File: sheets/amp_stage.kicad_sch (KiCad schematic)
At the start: 0 parts

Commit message: Complete Sheet 4 - Amp Stage TAS3251
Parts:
- added C34, C35, C38, C39, C40, C41, C42, C43, C44, C45: 1uF, symbol Device:C
- added C36, C37: 100nF, symbol Device:C
- added C46, C47, C48, C49: 33nF, symbol Device:C
- added C50, C51, C52, C53: 0.68µF, symbol Device:C
- added C54: 10nF, symbol Device:C
- added J2: Speaker Terminals, symbol Connector:Screw_Terminal_01x04
- added L4, L5, L6, L7: 15µH, symbol Device:L
- added R28, R29, R30, R31: 0.15, symbol Device:R
- added R32: 27K, symbol Device:R
- added R33: 10K, symbol Device:R
- added U10: TAS3251DKQR, DKQ0056A, symbol poe-aes67-amp:TAS3251DKQR
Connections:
- new net: C53.2, R31.1
- new net: R33.1, U10.18 (FREQ_ADJ)
- new net: C46.2, L4.1, U10.41 (SPK_OUTA+)
- new net: C45.1, U10.8 (CP)
- new net: C45.2, U10.6 (CN)
- new net: C51.2, R29.1
- new net: C47.1, U10.43 (BST_A-)
- new net: C47.2, L5.1, U10.39 (SPK_OUTA-)
- new net: C37.2, U10.12 (GVDD_A)
- new net: C48.2, L6.1, U10.36 (SPK_OUTB+)
- new net: C50.2, R28.1
- new net: U10.10 (DGND), U10.55 (AGND)
- new net: C40.2, U10.11 (DVDD_REG)
- new net: R32.2, U10.17 (OC_ADJ)
- new net: C39.2, U10.21 (DVDD)
- new net: C38.2, U10.23 (AVDD)
- new net: C54.1, U10.24 (C_START)
- new net: C36.2, U10.30 (GVDD_B)
- new net: C49.1, U10.31 (BST_B-)
- new net: C48.1, U10.32 (BST_B+)
- new net: C49.2, L7.1, U10.34 (SPK_OUTB-)
- new net: C46.1, U10.44 (BST_A+)
- new net: C41.1, U10.5 (CPVSS)
- new net: C52.2, R30.1
- new net +3.3V: C42.1, C43.1, C44.1, U10.52 (DAC_DVDD), U10.56 (DAC_AVDD), U10.9 (DAC_DVDD)
- new net AMP_CLIP (Output): U10.29 (CLIP_OTW_N)
- new net AMP_FAULT (Output): U10.28 (FAULT_N)
- new net AMP_MUTE (Input): U10.45 (DAC_MUTE_N)
- new net AMP_RESET (Input): U10.27 (RESET_AMP_N)
- new net GND: C34.1, C35.1, C36.1, C37.1, C38.1, C39.1, C40.1, C41.2, C42.2, C43.2, C44.2, C54.2, R28.2, R29.2, R30.2, R31.2, R32.1, R33.2, U10.13 (GND), U10.14 (MODE), U10.22 (GND), U10.33 (GND), U10.37 (GND), U10.38 (GND), U10.42 (GND), U10.46 (ADR), U10.7 (GND)
- new net I2C_SCL: U10.53 (SCL)
- new net I2C_SDA: U10.54 (SDA)
- new net I2S_BCLK: U10.49 (SCLK)
- new net I2S_LRCK: U10.47 (LRCK)
- new net I2S_MCLK: U10.50 (MCLK)
- new net I2S_SDIN: U10.48 (SDIN)
- new net I2S_SDOUT: U10.51 (SDOUT)
- new net OUTA_N: C50.1, J2.2 (Pin_2), L5.2
- new net OUTA_P: C51.1, J2.1 (Pin_1), L4.2
- new net OUTB_N: C52.1, J2.4 (Pin_4), L7.2
- new net OUTB_P: C53.1, J2.3 (Pin_3), L6.2
- new net V34: C34.2, C35.2, U10.35 (PVDD_B), U10.40 (PVDD_A)
- no-connect marks 0 -> 10

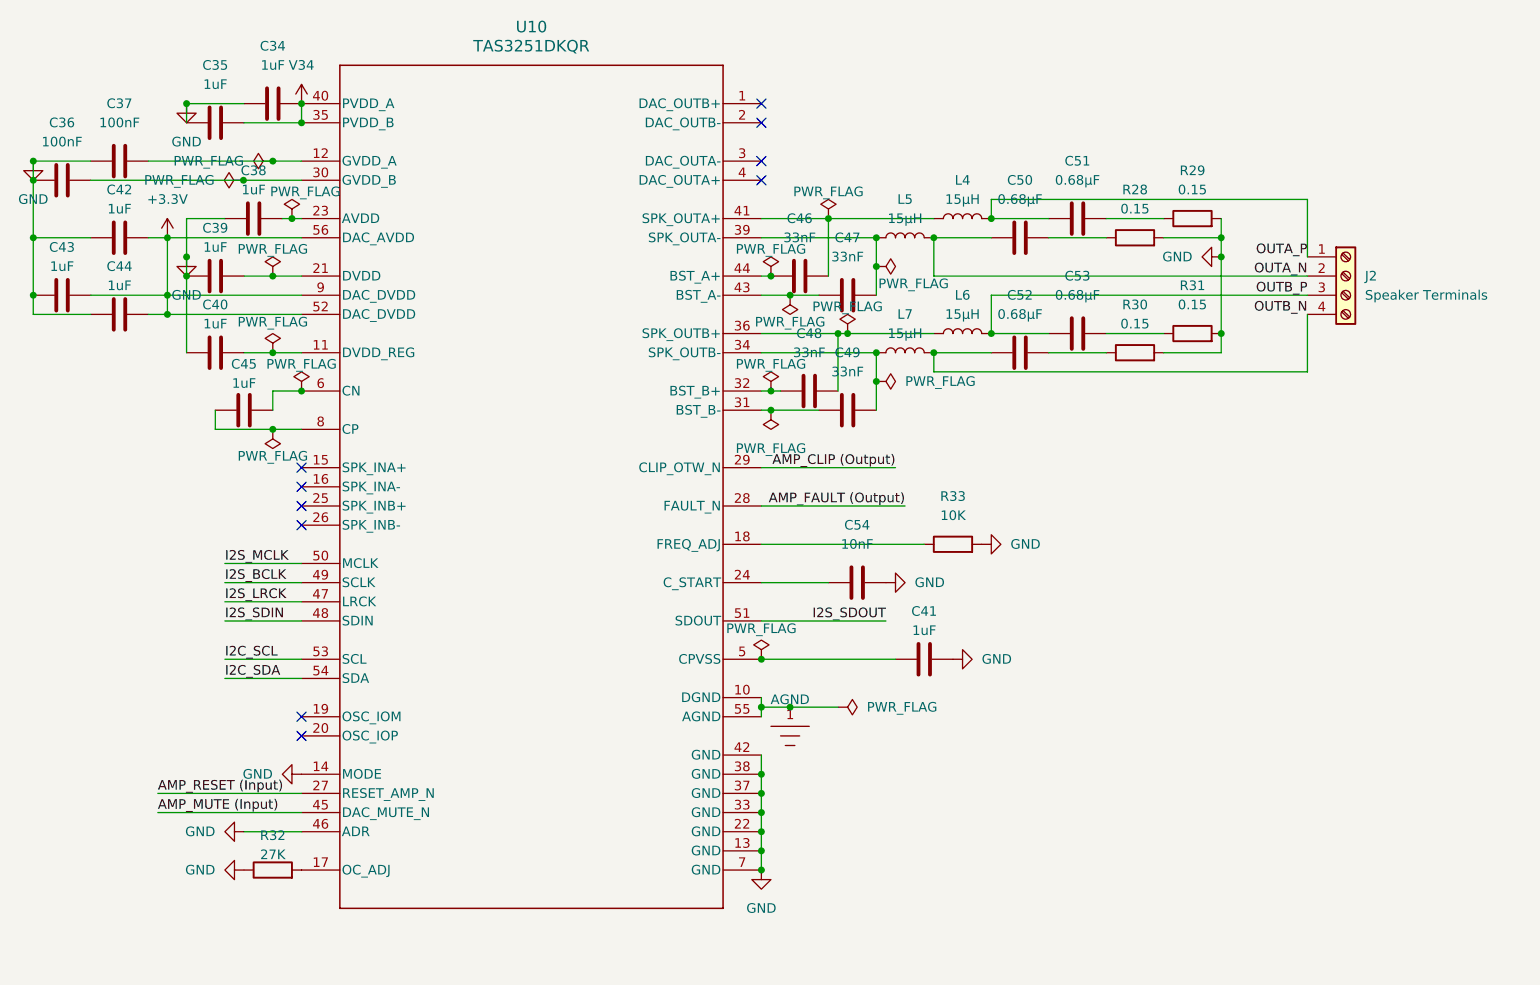
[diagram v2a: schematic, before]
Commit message: Complete datasheet audit and fixes across Sheets 2, 3 and 4
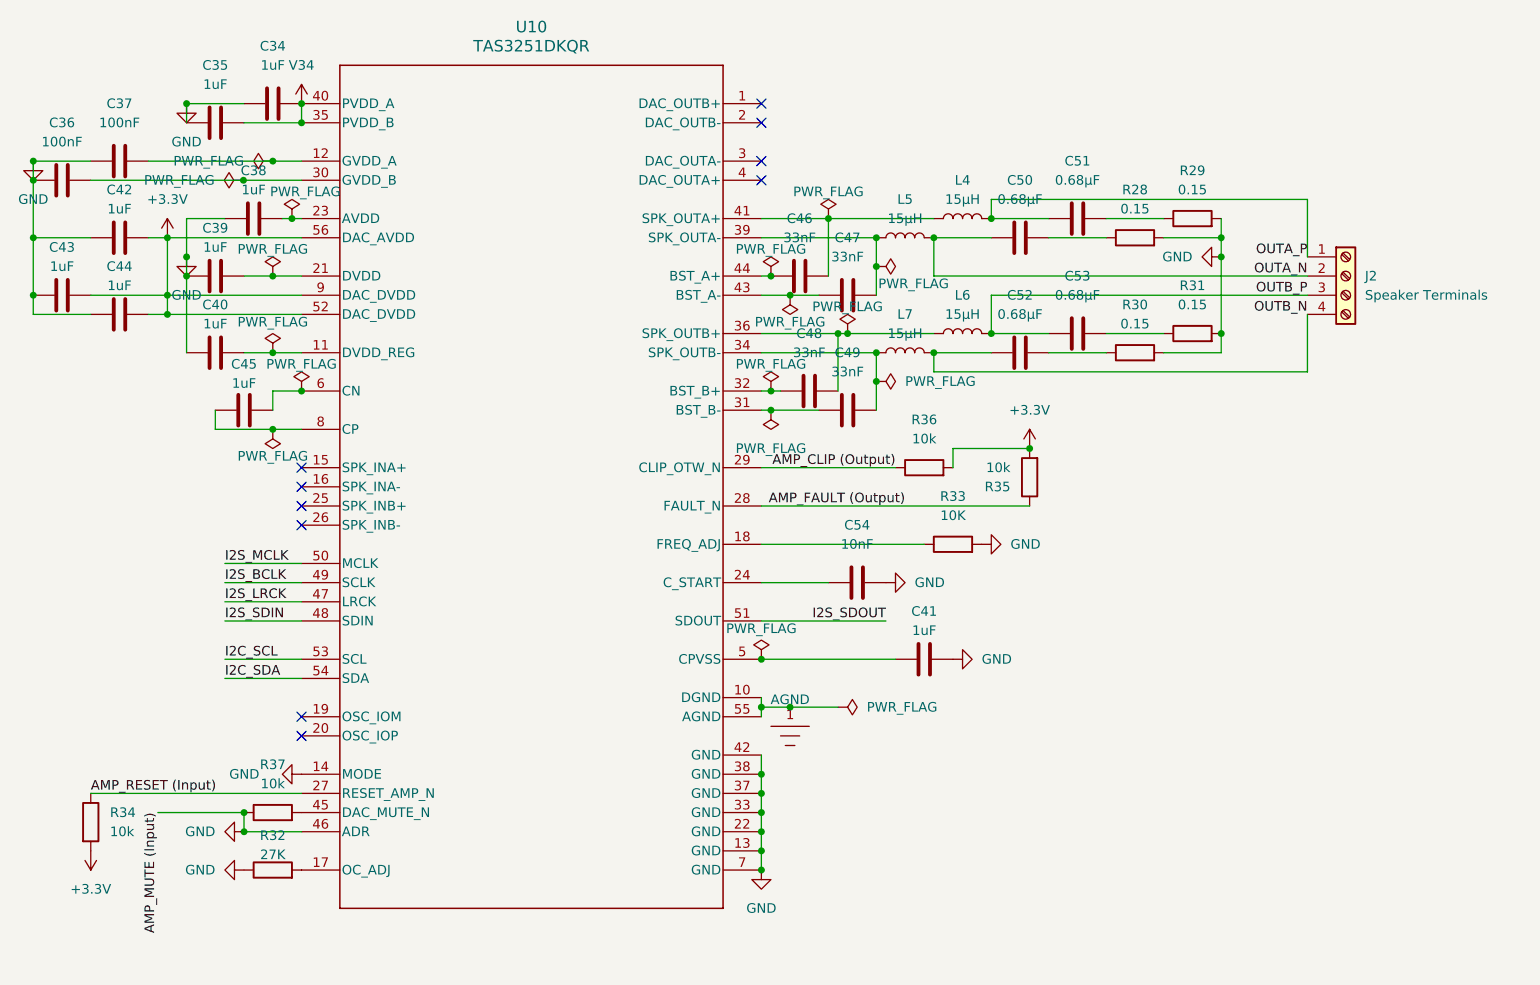
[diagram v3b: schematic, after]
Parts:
- added R34, R35, R36, R37: 10k, symbol Device:R
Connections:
- net +3.3V: now also R34.2, R35.2, R36.2
- net AMP_CLIP (Output): now also R36.1
- net AMP_FAULT (Output): now also R35.1
- net AMP_RESET (Input): now also R34.1
- net GND: now also R37.1
- net AMP_MUTE (Input): no longer names the net of U10.45 (DAC_MUTE_N)
- net AMP_MUTE (Input): now also R37.2
